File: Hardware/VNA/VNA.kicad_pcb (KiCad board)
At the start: 2 copper layers, 129 parts, among them J1 USB_B_Micro, J2 USB_A, J3 SMA, J4 SMA, U1 MAX2871, U10 SN74LVC1G139, U11 PE42440, U12 PE4257, U13 AD8302, U2 TVL755P, U3 LP5912, U4 MIC5366-1.8, U5 AD8319, U6 PE43711, U7 TRF37A75, U8 74AHC1G04, U9 PE42440, X1 ASTXR-12-19.200MHz

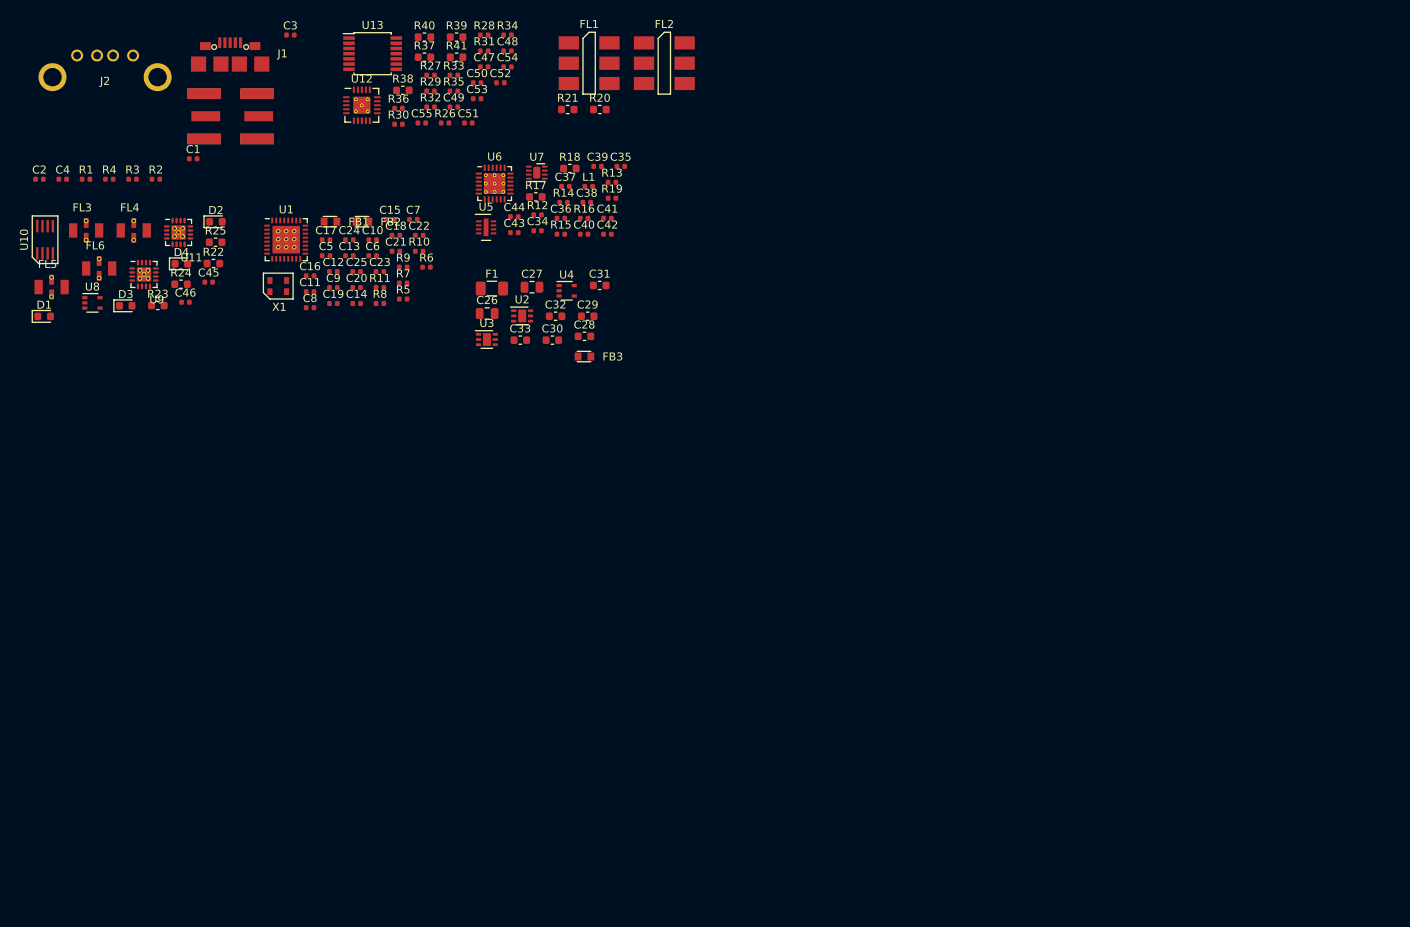
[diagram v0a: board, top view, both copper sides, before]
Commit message: all 3d models created, prelim bom generated
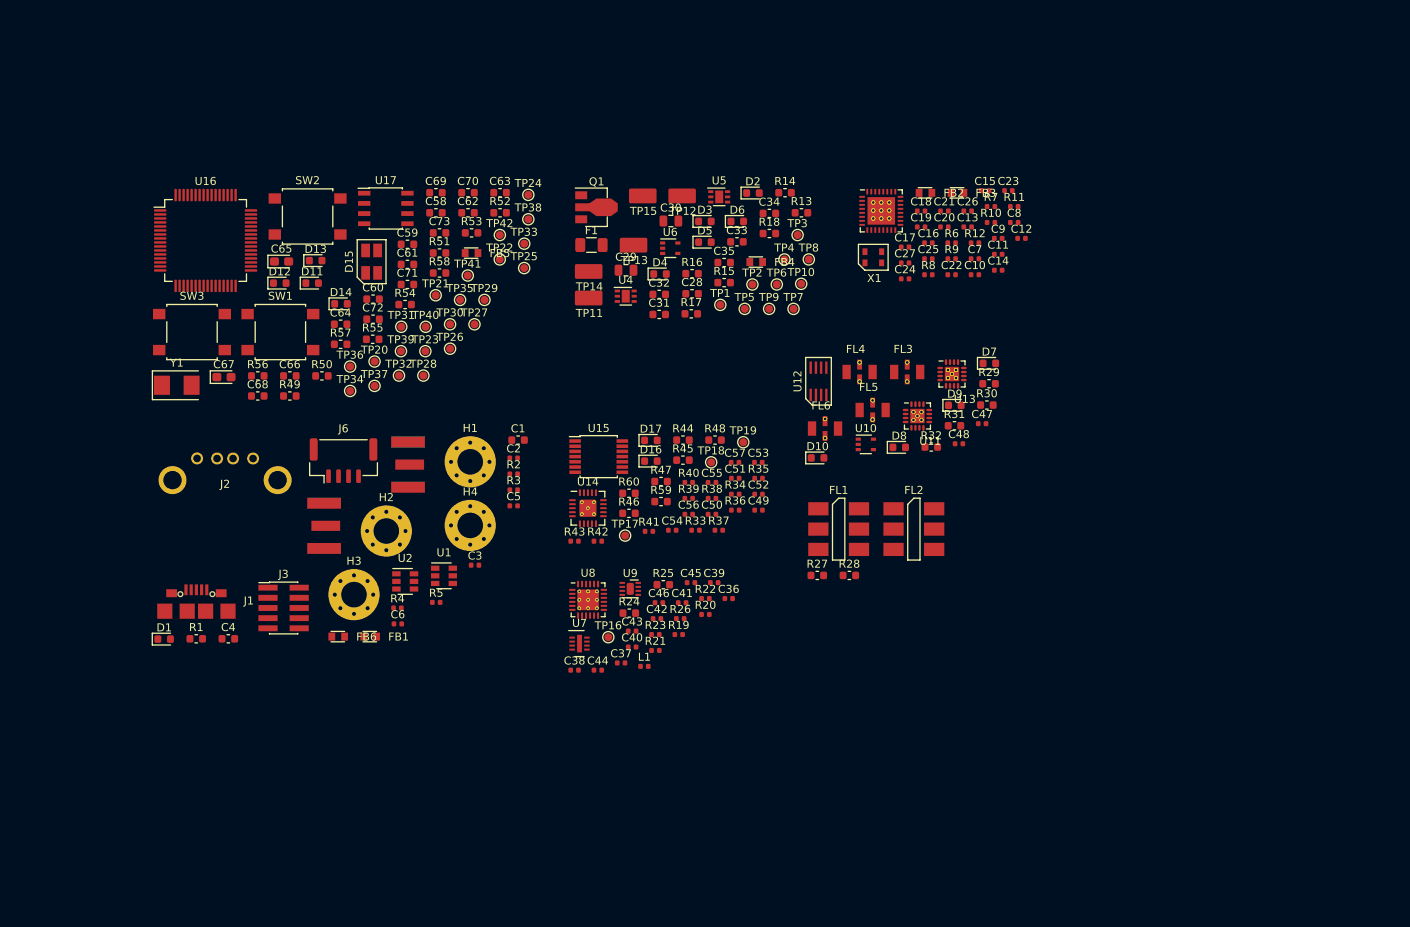
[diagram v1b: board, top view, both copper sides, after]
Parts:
- added C56: 100p, Capacitor_SMD:C_0402_1005Metric, F.Cu at (102.1, 78.8)
- added C57: DNP, Capacitor_SMD:C_0402_1005Metric, F.Cu at (107.9, 72.3)
- added C58: 1u, Capacitor_SMD:C_0603_1608Metric, F.Cu at (70.5, 41.1)
- added C59: 100n, Capacitor_SMD:C_0603_1608Metric, F.Cu at (67.0, 45.0)
- added C60: 10p, Capacitor_SMD:C_0603_1608Metric, F.Cu at (62.7, 51.9)
- added C61: 10p, Capacitor_SMD:C_0603_1608Metric, F.Cu at (67.0, 47.5)
- added C62: 1u, Capacitor_SMD:C_0603_1608Metric, F.Cu at (74.5, 41.1)
- added C63: 100n, Capacitor_SMD:C_0603_1608Metric, F.Cu at (78.5, 38.6)
- added C64: 100n, Capacitor_SMD:C_0603_1608Metric, F.Cu at (58.6, 55.0)
- added C65: 1u, Capacitor_Tantalum_SMD:CP_EIA-2012-15_AVX-P, F.Cu at (51.2, 47.2)
- added C66: 100n, Capacitor_SMD:C_0603_1608Metric, F.Cu at (52.3, 61.5)
- added C67: 1u, Capacitor_Tantalum_SMD:CP_EIA-2012-15_AVX-P, F.Cu at (44.0, 61.6)
- added C68: 100n, Capacitor_SMD:C_0603_1608Metric, F.Cu at (48.2, 64.0)
- added C69: 1u, Capacitor_SMD:C_0603_1608Metric, F.Cu at (70.5, 38.6)
- added C70: 100n, Capacitor_SMD:C_0603_1608Metric, F.Cu at (74.5, 38.6)
- added C71: 1u, Capacitor_SMD:C_0603_1608Metric, F.Cu at (67.0, 50.0)
- added C72: 100n, Capacitor_SMD:C_0603_1608Metric, F.Cu at (62.7, 54.4)
- added C73: 100n, Capacitor_SMD:C_0603_1608Metric, F.Cu at (71.0, 43.6)
- added D10: LED, LED_SMD:LED_0603_1608Metric, F.Cu at (118.2, 71.7)
- added D11: LED, LED_SMD:LED_0603_1608Metric, F.Cu at (55.0, 49.9)
- added D12: LED, LED_SMD:LED_0603_1608Metric, F.Cu at (51.0, 49.9)
- added D13: LED, LED_SMD:LED_0603_1608Metric, F.Cu at (55.5, 47.0)
- added D14: LED, LED_SMD:LED_0603_1608Metric, F.Cu at (58.6, 52.4)
- added D15: LED_RGBA, VNA_Footprints:ARGB_PLCC4_1210_LED, F.Cu at (62.5, 47.2)
- added D16: LED, LED_SMD:LED_0603_1608Metric, F.Cu at (97.4, 72.1)
- added D17: LED, LED_SMD:LED_0603_1608Metric, F.Cu at (97.4, 69.5)
- added D5: LED, LED_SMD:LED_0603_1608Metric, F.Cu at (104.1, 44.7)
- added D6: LED, LED_SMD:LED_0603_1608Metric, F.Cu at (108.2, 42.1)
- added D7: LED, LED_SMD:LED_0603_1608Metric, F.Cu at (139.7, 59.9)
- added D8: LED, LED_SMD:LED_0603_1608Metric, F.Cu at (128.4, 70.4)
- added D9: LED, LED_SMD:LED_0603_1608Metric, F.Cu at (135.4, 65.1)
- added FB4: Bead, VNA_Footprints:BEADC1608X95N, F.Cu at (110.6, 47.2)
- added FB5: Bead, VNA_Footprints:BEADC1608X95N, F.Cu at (75.0, 46.1)
- added FB6: Bead, VNA_Footprints:BEADC1608X95N, F.Cu at (58.3, 94.0)
- added H1: M3_Via_Pad, MountingHole:MountingHole_3.2mm_M3_Pad_Via, F.Cu at (74.8, 72.2)
- added H2: M3_Via_Pad, MountingHole:MountingHole_3.2mm_M3_Pad_Via, F.Cu at (64.3, 80.8)
- added H3: M3_Via_Pad, MountingHole:MountingHole_3.2mm_M3_Pad_Via, F.Cu at (60.3, 88.8)
- added H4: M3_Via_Pad, MountingHole:MountingHole_3.2mm_M3_Pad_Via, F.Cu at (74.8, 80.1)
- added J5: SMA, VNA_Footprints:SMA_EDGE_MOUNT, F.Cu at (56.5, 80.2)
- added J6: UART, Connector_JST:JST_GH_BM04B-GHS-TBT_1x04-1MP_P1.25mm_Vertical, F.Cu at (59.0, 72.0)
- added Q1: RE1C002UN, Package_TO_SOT_SMD:SOT-89-3, F.Cu at (90.2, 40.4)
- added R42: 52R3, Resistor_SMD:R_0402_1005Metric, F.Cu at (90.8, 82.1)
- added R43: 52R3, Resistor_SMD:R_0402_1005Metric, F.Cu at (87.8, 82.1)
- added R44: 0R0, Resistor_SMD:R_0603_1608Metric, F.Cu at (101.4, 69.5)
- added R45: 0R0, Resistor_SMD:R_0603_1608Metric, F.Cu at (101.4, 72.0)
- added R46: 0R0, Resistor_SMD:R_0603_1608Metric, F.Cu at (94.6, 78.6)
- added R47: 0R0, Resistor_SMD:R_0603_1608Metric, F.Cu at (98.7, 74.7)
- added R48: 0R0, Resistor_SMD:R_0603_1608Metric, F.Cu at (105.4, 69.5)
- added R49: DNP, Resistor_SMD:R_0603_1608Metric, F.Cu at (52.3, 64.0)
- added R50: 10K, Resistor_SMD:R_0603_1608Metric, F.Cu at (56.3, 61.5)
- added R51: 0R0, Resistor_SMD:R_0603_1608Metric, F.Cu at (71.0, 46.1)
- added R52: 470R, Resistor_SMD:R_0603_1608Metric, F.Cu at (78.5, 41.1)
- added R53: 470R, Resistor_SMD:R_0603_1608Metric, F.Cu at (75.0, 43.6)
- added R54: 470R, Resistor_SMD:R_0603_1608Metric, F.Cu at (66.7, 52.5)
- added R55: 470R, Resistor_SMD:R_0603_1608Metric, F.Cu at (62.6, 56.9)
- added R56: 0R0, Resistor_SMD:R_0603_1608Metric, F.Cu at (48.2, 61.5)
- added R57: 0R0, Resistor_SMD:R_0603_1608Metric, F.Cu at (58.6, 57.5)
- added R58: 1K5, Resistor_SMD:R_0603_1608Metric, F.Cu at (71.0, 48.6)
- added R59: 470R, Resistor_SMD:R_0603_1608Metric, F.Cu at (98.7, 77.2)
- added R60: 470R, Resistor_SMD:R_0603_1608Metric, F.Cu at (94.6, 76.1)
- added SW1: SW_Push, VNA_Footprints:6mmTactSwitch, F.Cu at (51.1, 56.0)
- added SW2: SW_Push, VNA_Footprints:6mmTactSwitch, F.Cu at (54.5, 41.5)
- added SW3: SW_Push, VNA_Footprints:6mmTactSwitch, F.Cu at (40.0, 56.0)
- added TP1: VBUS, TestPoint:TestPoint_Pad_D1.0mm, F.Cu at (106.1, 52.6)
- added TP10: GND, TestPoint:TestPoint_Pad_D1.0mm, F.Cu at (116.2, 49.9)
- added TP11: GND, VNA_Footprints:S1751-46_smdTestPoint, F.Cu at (89.6, 51.7)
- added TP12: GND, VNA_Footprints:S1751-46_smdTestPoint, F.Cu at (101.3, 39.0)
- added TP13: GND, VNA_Footprints:S1751-46_smdTestPoint, F.Cu at (95.2, 45.1)
- added TP14: GND, VNA_Footprints:S1751-46_smdTestPoint, F.Cu at (89.6, 48.4)
- added TP15: GND, VNA_Footprints:S1751-46_smdTestPoint, F.Cu at (96.4, 39.0)
- added TP16: TP, TestPoint:TestPoint_Pad_D1.0mm, F.Cu at (92.1, 94.1)
- added TP17: TP, TestPoint:TestPoint_Pad_D1.0mm, F.Cu at (94.2, 81.4)
- added TP18: TP, TestPoint:TestPoint_Pad_D1.0mm, F.Cu at (104.9, 72.3)
- added TP19: TP, TestPoint:TestPoint_Pad_D1.0mm, F.Cu at (108.9, 69.7)
- added TP2: 5V0, TestPoint:TestPoint_Pad_D1.0mm, F.Cu at (110.1, 50.0)
- added TP20: TP, TestPoint:TestPoint_Pad_D1.0mm, F.Cu at (62.8, 59.7)
- added TP21: TP, TestPoint:TestPoint_Pad_D1.0mm, F.Cu at (70.5, 51.4)
- added TP22: TP, TestPoint:TestPoint_Pad_D1.0mm, F.Cu at (78.5, 46.9)
- added TP23: TP, TestPoint:TestPoint_Pad_D1.0mm, F.Cu at (69.2, 58.4)
- added TP24: TP, TestPoint:TestPoint_Pad_D1.0mm, F.Cu at (82.1, 38.8)
- added TP25: TP, TestPoint:TestPoint_Pad_D1.0mm, F.Cu at (81.5, 48.0)
- added TP26: TP, TestPoint:TestPoint_Pad_D1.0mm, F.Cu at (72.3, 58.1)
- added TP27: TP, TestPoint:TestPoint_Pad_D1.0mm, F.Cu at (75.3, 55.0)
- added TP28: TP, TestPoint:TestPoint_Pad_D1.0mm, F.Cu at (68.9, 61.4)
- added TP29: TP, TestPoint:TestPoint_Pad_D1.0mm, F.Cu at (76.6, 52.0)
- added TP3: 3V3A, TestPoint:TestPoint_Pad_D1.0mm, F.Cu at (115.7, 43.8)
- added TP30: TP, TestPoint:TestPoint_Pad_D1.0mm, F.Cu at (72.3, 55.0)
- added TP31: TP, TestPoint:TestPoint_Pad_D1.0mm, F.Cu at (66.2, 55.3)
- added TP32: TP, TestPoint:TestPoint_Pad_D1.0mm, F.Cu at (65.9, 61.4)
- added TP33: TP, TestPoint:TestPoint_Pad_D1.0mm, F.Cu at (81.6, 44.9)
- added TP34: TP, TestPoint:TestPoint_Pad_D1.0mm, F.Cu at (59.8, 63.3)
- added TP35: TP, TestPoint:TestPoint_Pad_D1.0mm, F.Cu at (73.5, 52.0)
- added TP36: TP, TestPoint:TestPoint_Pad_D1.0mm, F.Cu at (59.8, 60.3)
- added TP37: TP, TestPoint:TestPoint_Pad_D1.0mm, F.Cu at (62.8, 62.7)
- added TP38: TP, TestPoint:TestPoint_Pad_D1.0mm, F.Cu at (82.1, 41.9)
- added TP39: TP, TestPoint:TestPoint_Pad_D1.0mm, F.Cu at (66.1, 58.4)
- added TP4: 1V8, TestPoint:TestPoint_Pad_D1.0mm, F.Cu at (114.1, 46.9)
- added TP40: TP, TestPoint:TestPoint_Pad_D1.0mm, F.Cu at (69.2, 55.3)
- added TP41: TP, TestPoint:TestPoint_Pad_D1.0mm, F.Cu at (74.5, 48.9)
- added TP42: TP, TestPoint:TestPoint_Pad_D1.0mm, F.Cu at (78.5, 43.8)
- added TP5: 3V3, TestPoint:TestPoint_Pad_D1.0mm, F.Cu at (109.1, 53.1)
- added TP6: GND, TestPoint:TestPoint_Pad_D1.0mm, F.Cu at (113.1, 50.0)
- added TP7: GND, TestPoint:TestPoint_Pad_D1.0mm, F.Cu at (115.2, 53.1)
- added TP8: GND, TestPoint:TestPoint_Pad_D1.0mm, F.Cu at (117.1, 46.9)
- added TP9: GND, TestPoint:TestPoint_Pad_D1.0mm, F.Cu at (112.2, 53.1)
- added U14: PE4257, VNA_Footprints:QFN-20-1EP_4x4mm_P0.5mm_EP2.15x2.15mm_ThermalVias, F.Cu at (89.5, 78.0)
- added U15: AD8302, Package_SO:TSSOP-14_4.4x5mm_P0.65mm, F.Cu at (90.9, 71.5)
- added U16: STM32F373RCTx, Package_QFP:LQFP-64_10x10mm_P0.5mm, F.Cu at (41.7, 44.5)
- added U17: AT25SF081-SSHD-X, Package_SO:SOIC-8_3.9x4.9mm_P1.27mm, F.Cu at (64.3, 40.5)
- added Y1: 8MHz, VNA_Footprints:Crystal_SMD_5032-2Pin_5.0x3.2mm, F.Cu at (38.1, 62.6)
- C1, C4: value 1n -> 100n; footprint Capacitor_SMD:C_0402_1005Metric -> Capacitor_SMD:C_0603_1608Metric
- C10: value 10n -> 1u
- C11: value 100p -> 1u
- C22: value 100n -> 10n
- C23: value 12n -> 100p
- C24: value 820p -> 100n
- C25: value 100p -> 12n
- C26: value 10u -> 820p; footprint Capacitor_SMD:C_0805_2012Metric -> Capacitor_SMD:C_0402_1005Metric
- C27: value 10u -> 100p; footprint Capacitor_SMD:C_0805_2012Metric -> Capacitor_SMD:C_0402_1005Metric
- C29, C30: value 1u -> 10u; footprint Capacitor_SMD:C_0603_1608Metric -> Capacitor_SMD:C_0805_2012Metric
- C34: value 8.2p -> 1u; footprint Capacitor_SMD:C_0402_1005Metric -> Capacitor_SMD:C_0603_1608Metric
- C35: value 47n -> 1u; footprint Capacitor_SMD:C_0402_1005Metric -> Capacitor_SMD:C_0603_1608Metric
- C36: value 100n -> 8.2p
- C37, C40: value 100p -> 47n
- C38: value 47n -> 100n
- C39: value 100n -> 100p
- C41: value 1n -> 100n
- C42: value 10n -> 100p
- C43, C6: value 10n -> 1n
- C44: value 10p -> 10n
- C46: value 10n -> 10p
- C48, C49: value 1n -> 10n
- C5, C53: value 100n -> 1n
- C52: value DNP -> 1n
- C54: value 100p -> DNP
- C55: value DNP -> 100n
- C7: value 1u -> 100n
- C8: value 1u -> 10n
- F1: footprint Fuse:Fuse_1206_3216Metric -> VNA_Footprints:Fuse_1206_3216Metric
- FB1, FB2, FB3: value BLM18PG181SN1D -> Bead
- J3: value SMA -> Conn_ARM_SWD; footprint VNA_Footprints:SMA_EDGE_MOUNT -> VNA_Footprints:SAMTEC_FTSH-105-01-L-DV-R-TR
- R1: value 49R9 -> 470R; footprint Resistor_SMD:R_0402_1005Metric -> Resistor_SMD:R_0603_1608Metric
- R10: value 240 -> 31.1
- R11: value 49.9 -> 240
- R12: value 18k -> 49.9
- R13: value 52.3 -> 10K; footprint Resistor_SMD:R_0402_1005Metric -> Resistor_SMD:R_0603_1608Metric
- R14: value 0 -> 470R; footprint Resistor_SMD:R_0402_1005Metric -> Resistor_SMD:R_0603_1608Metric
- R15: value OPT -> 470R; footprint Resistor_SMD:R_0402_1005Metric -> Resistor_SMD:R_0603_1608Metric
- R16: value 1k -> 470R; footprint Resistor_SMD:R_0402_1005Metric -> Resistor_SMD:R_0603_1608Metric
- R17: value 0R -> 1K
- R18: value DNP -> 1K
- R19: value 1R8 -> 18k
- R2: value 16R6 -> 49R9
- R20: value 49R9 -> 52.3; footprint Resistor_SMD:R_0603_1608Metric -> Resistor_SMD:R_0402_1005Metric
- R21: value 49R9 -> 0; footprint Resistor_SMD:R_0603_1608Metric -> Resistor_SMD:R_0402_1005Metric
- R22: value 470R -> OPT; footprint Resistor_SMD:R_0603_1608Metric -> Resistor_SMD:R_0402_1005Metric
- R23: value 470R -> 1k; footprint Resistor_SMD:R_0603_1608Metric -> Resistor_SMD:R_0402_1005Metric
- R24: value 470R -> 0R
- R25: value 470R -> DNP
- R26: value DNP -> 1R8
- R27: value 150R -> 49R9; footprint Resistor_SMD:R_0402_1005Metric -> Resistor_SMD:R_0603_1608Metric
- R28: value 60R -> 49R9; footprint Resistor_SMD:R_0402_1005Metric -> Resistor_SMD:R_0603_1608Metric
- R29: value 0R0 -> 470R; footprint Resistor_SMD:R_0402_1005Metric -> Resistor_SMD:R_0603_1608Metric
- R30: value 37R -> 470R; footprint Resistor_SMD:R_0402_1005Metric -> Resistor_SMD:R_0603_1608Metric
- R31: value 278R -> 470R; footprint Resistor_SMD:R_0402_1005Metric -> Resistor_SMD:R_0603_1608Metric
- R32: value DNP -> 470R; footprint Resistor_SMD:R_0402_1005Metric -> Resistor_SMD:R_0603_1608Metric
- R33: value 150R -> DNP
- R34: value 60R -> 150R
- R35: value 52R3 -> 60R
- R36: value 52R3 -> 0R0
- R37: value 0R0 -> 37R; footprint Resistor_SMD:R_0603_1608Metric -> Resistor_SMD:R_0402_1005Metric
- R38: value 0R0 -> 278R; footprint Resistor_SMD:R_0603_1608Metric -> Resistor_SMD:R_0402_1005Metric
- R39: value 0R0 -> DNP; footprint Resistor_SMD:R_0603_1608Metric -> Resistor_SMD:R_0402_1005Metric
- R40: value 0R0 -> 150R; footprint Resistor_SMD:R_0603_1608Metric -> Resistor_SMD:R_0402_1005Metric
- R41: value 0R0 -> 60R; footprint Resistor_SMD:R_0603_1608Metric -> Resistor_SMD:R_0402_1005Metric
- R5: value 5.1k -> 16R6
- R6: value 0 -> 5.1k
- R8: value 90.9 -> 0
- R9: value 31.1 -> 90.9
- U1: value MAX2871 -> TPD2S017; footprint VNA_Footprints:QFN-32-1EP_5x5mm_Pitch0.5mm_Thermal_Vias -> Package_TO_SOT_SMD:SOT-23-6
- U10: value SN74LVC1G139 -> 74AHC1G04; footprint VNA_Footprints:VSSOP-8_2.9x3.15mm_P0.65 -> Package_TO_SOT_SMD:SOT-353_SC-70-5
- U12: value PE4257 -> SN74LVC1G139; footprint VNA_Footprints:QFN-20-1EP_4x4mm_P0.5mm_EP2.15x2.15mm_ThermalVias -> VNA_Footprints:VSSOP-8_2.9x3.15mm_P0.65
- U13: value AD8302 -> PE42440; footprint Package_SO:TSSOP-14_4.4x5mm_P0.65mm -> VNA_Footprints:QFN-16-1EP_3x3mm_P0.5mm_EP2.7x2.7mm_ThermalVias
- U2: value TVL755P -> TPD2S017; footprint Package_DFN_QFN:DFN-6-1EP_2x2mm_P0.65mm_EP1x1.6mm -> Package_TO_SOT_SMD:SOT-23-6
- U3: value LP5912 -> MAX2871; footprint Package_DFN_QFN:DFN-6-1EP_2x2mm_P0.65mm_EP1x1.6mm -> VNA_Footprints:QFN-32-1EP_5x5mm_Pitch0.5mm_Thermal_Vias
- U4: value MIC5366-1.8 -> LP5912; footprint Package_TO_SOT_SMD:SOT-353_SC-70-5 -> Package_DFN_QFN:DFN-6-1EP_2x2mm_P0.65mm_EP1x1.6mm
- U5: value AD8319 -> TVL755P; footprint Package_DFN_QFN:DFN-8-1EP_2x3mm_P0.5mm_EP0.61x2.2mm -> Package_DFN_QFN:DFN-6-1EP_2x2mm_P0.65mm_EP1x1.6mm
- U6: value PE43711 -> MIC5366-1.8; footprint VNA_Footprints:QFN-24-1EP_4x4mm_P0.5mm_EP2.7x2.6mm_ThermalVias -> Package_TO_SOT_SMD:SOT-353_SC-70-5
- U7: value TRF37A75 -> AD8319; footprint Package_DFN_QFN:DFN-8-1EP_2x2mm_P0.5mm_EP0.9x1.5mm -> Package_DFN_QFN:DFN-8-1EP_2x3mm_P0.5mm_EP0.61x2.2mm
- U8: value 74AHC1G04 -> PE43711; footprint Package_TO_SOT_SMD:SOT-353_SC-70-5 -> VNA_Footprints:QFN-24-1EP_4x4mm_P0.5mm_EP2.7x2.6mm_ThermalVias
- U9: value PE42440 -> TRF37A75; footprint VNA_Footprints:QFN-16-1EP_3x3mm_P0.5mm_EP2.7x2.7mm_ThermalVias -> Package_DFN_QFN:DFN-8-1EP_2x2mm_P0.5mm_EP0.9x1.5mm
- moved U10 105.7 mm to (124.3, 70.0)
- moved FL3 104.1 mm to (129.4, 61.0)
- moved FL5 103.8 mm to (125.1, 65.7)
- moved U11 95.2 mm to (130.7, 66.5)
- moved FL6 92.9 mm to (119.2, 68.0)
- moved FL4 92.4 mm to (123.5, 61.0)
- moved C8 88.7 mm to (142.8, 42.3)
- moved C11 86.1 mm to (140.8, 46.3)
- moved C12 86.1 mm to (143.7, 44.3)
- moved C9 83.3 mm to (140.8, 44.3)
- moved U13 82.8 mm to (135.0, 61.2)
- moved R28 81.5 mm to (122.2, 86.4)
- moved R30 81.5 mm to (139.4, 65.1)
- moved C14 80.3 mm to (140.8, 48.2)
- moved R11 79.9 mm to (142.8, 40.3)
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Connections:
- C1 pad 2: /Synth/RF_OUT_N -> GND
- C10 pad 1: /3V3 -> Net-(C10-Pad1)
- C11 pad 1: /3V3 -> Net-(C11-Pad1)
- C12 pad 1: /3V3 -> VDD
- C13 pad 1: /3V3 -> VDD
- C14 pad 1: Net-(C14-Pad1) -> VDD
- C15 pad 1: Net-(C14-Pad1) -> VDD
- C16 pad 1: Net-(C14-Pad1) -> Net-(C16-Pad1)
- C17 pad 1: Net-(C14-Pad1) -> Net-(C16-Pad1)
- C18 pad 1: Net-(C18-Pad1) -> Net-(C16-Pad1)
- C19 pad 1: Net-(C18-Pad1) -> Net-(C16-Pad1)
- C2 pad 1: /Filter Bank/RF_IN -> Net-(C2-Pad1)
- C2 pad 2: /Synth/RF_OUT_P -> /Synth/RF_OUT_N
- C20 pad 1: Net-(C18-Pad1) -> Net-(C20-Pad1)
- C21 pad 1: Net-(C18-Pad1) -> Net-(C20-Pad1)
- C22 pad 1: Net-(C22-Pad1) -> Net-(C20-Pad1)
- C22 pad 2: Net-(C22-Pad2) -> GND
- C23 pad 1: Net-(C22-Pad2) -> Net-(C20-Pad1)
- C24 pad 2: GND -> Net-(C24-Pad2)
- C25 pad 1: /3V3A -> Net-(C24-Pad2)
- C26 pad 1: /Power/VIN -> Net-(C26-Pad1)
- C27 pad 1: /5V0 -> /3V3A
- C29 pad 1: /3V3 -> /Power/VIN
- C3 pad 1: /Source Leveling/RF_IN -> /Filter Bank/RF_IN
- C3 pad 2: /Filter Bank/RF_OUT -> /Synth/RF_OUT_P
- C30 pad 1: /Power/VIN -> /5V0
- C32 pad 1: /3V3A -> /Power/VIN
- C33 pad 1: /1V8 -> /3V3A
- C34 pad 1: Net-(C34-Pad1) -> VDD
- C35 pad 1: /AD8319_RF -> /1V8
- C35 pad 2: Net-(C35-Pad2) -> GND
- C36 pad 1: GND -> Net-(C36-Pad1)
- C36 pad 2: /3V3A -> GND
- C37 pad 1: GND -> /AD8319_RF
- C37 pad 2: /3V3A -> Net-(C37-Pad2)
- C38 pad 2: Net-(C38-Pad2) -> /3V3A
- C4 pad 1: /Directional Couplers/RF_IN -> Net-(C4-Pad1)
- C4 pad 2: /Source Leveling/RF_OUT -> GND
- C40 pad 2: /3V3A -> Net-(C40-Pad2)
- C41 pad 1: Net-(C41-Pad1) -> GND
- C41 pad 2: Net-(C41-Pad2) -> /3V3A
- C42 pad 1: /5V0 -> GND
- C42 pad 2: GND -> /3V3A
- C43 pad 1: /5V0 -> Net-(C43-Pad1)
- C43 pad 2: GND -> Net-(C43-Pad2)
- C44 pad 1: Net-(C44-Pad1) -> /5V0
- C45 pad 1: GND -> /5V0
- C45 pad 2: /3V3A -> GND
- C46 pad 1: GND -> Net-(C46-Pad1)
- C46 pad 2: /3V3A -> GND
- C47 pad 2: /3V3 -> /3V3A
- C48 pad 1: Net-(C48-Pad1) -> GND
- C48 pad 2: Net-(C48-Pad2) -> /3V3A
- C49 pad 1: Net-(C49-Pad1) -> GND
- C49 pad 2: GND -> /3V3A
- C5 pad 1: /1V8 -> /Source Leveling/RF_IN
- C5 pad 2: GND -> /Filter Bank/RF_OUT
- C50 pad 2: GND -> Net-(C50-Pad2)
- C51 pad 2: Net-(C51-Pad2) -> GND
- C53 pad 1: GND -> Net-(C53-Pad1)
- C53 pad 2: /3V3 -> Net-(C53-Pad2)
- C54 pad 1: GND -> Net-(C54-Pad1)
- C54 pad 2: /3V3 -> GND
- C55 pad 1: Net-(C55-Pad1) -> GND
- C55 pad 2: GND -> /3V3A
- C6 pad 1: Net-(C6-Pad1) -> /Directional Couplers/RF_IN
- C6 pad 2: Net-(C6-Pad2) -> /Source Leveling/RF_OUT
- C7 pad 1: Net-(C7-Pad1) -> /1V8
- C8 pad 2: GND -> Net-(C8-Pad2)
- D1 pad 1: Net-(D1-Pad1) -> GND
- D3 pad 1: Net-(D3-Pad1) -> GND
- D4 pad 1: Net-(D4-Pad1) -> GND
- FB1 pad 1: Net-(C14-Pad1) -> /VBUS
- FB1 pad 2: /3V3A -> Net-(C1-Pad1)
- FB2 pad 1: Net-(C18-Pad1) -> Net-(C16-Pad1)
- FB3 pad 1: /5V0 -> Net-(C20-Pad1)
- FB3 pad 2: /Power/VIN -> /3V3A
- J1 pad 1: /VBUS -> Net-(C1-Pad1)
- J1 pad 2: (no net) -> /Dn
- J1 pad 3: (no net) -> /Dp
- J2 pad 1: /5V0 -> Net-(C4-Pad1)
- J2 pad 2: (no net) -> Net-(J2-Pad2)
- J2 pad 3: (no net) -> Net-(J2-Pad3)
- J3 pad 1: /RF_THROUGH -> VDD
- J3 pad 2: GND -> /SWD_IO
- J4 pad 1: /Directional Couplers/RF_OUT -> /RF_THROUGH
- L1 pad 1: Net-(C44-Pad1) -> Net-(C46-Pad1)
- R1 pad 1: Net-(C1-Pad1) -> /MAX2871_LD
- R1 pad 2: GND -> Net-(D1-Pad2)
- R10 pad 1: Net-(C22-Pad2) -> Net-(R10-Pad1)
- R11 pad 1: /3V3A -> Net-(C24-Pad2)
- R11 pad 2: /Synth/RF_OUT_P -> Net-(C26-Pad1)
- R12 pad 1: Net-(R12-Pad1) -> /3V3A
- R12 pad 2: GND -> /Synth/RF_OUT_P
- R13 pad 1: GND -> /1V8
- R13 pad 2: /AD8319_RF -> GND
- R14 pad 1: Net-(R14-Pad1) -> /3V3A
- R14 pad 2: Net-(R14-Pad2) -> Net-(D2-Pad2)
- R15 pad 1: Net-(R14-Pad2) -> /3V3A
- R15 pad 2: GND -> Net-(D3-Pad2)
- R16 pad 1: (no net) -> VDD
- R16 pad 2: Net-(R14-Pad1) -> Net-(D4-Pad2)
- R17 pad 1: /3V3A -> /5V0
- R17 pad 2: /Source Leveling/nP_S -> Net-(D5-Pad2)
- R18 pad 1: /Source Leveling/nP_S -> /VBUS
- R18 pad 2: GND -> Net-(D6-Pad2)
- R19 pad 1: /5V0 -> Net-(R19-Pad1)
- R19 pad 2: Net-(C44-Pad1) -> GND
- R2 pad 1: Net-(R2-Pad1) -> Net-(C2-Pad1)
- R2 pad 2: /AD8319_RF -> GND
- R20 pad 1: Net-(FL1-Pad4) -> GND
- R20 pad 2: GND -> /AD8319_RF
- R21 pad 1: Net-(FL2-Pad4) -> Net-(R21-Pad1)
- R21 pad 2: GND -> Net-(R21-Pad2)
- R22 pad 1: Net-(D1-Pad2) -> Net-(R21-Pad2)
- R22 pad 2: /3V3 -> GND
- R23 pad 1: Net-(D2-Pad2) -> /RF_PWR_LEVEL
- R23 pad 2: /3V3 -> Net-(R21-Pad1)
- R24 pad 1: Net-(D3-Pad2) -> /3V3A
- R24 pad 2: /3V3 -> /Source Leveling/nP_S
- R25 pad 1: Net-(D4-Pad2) -> /Source Leveling/nP_S
- R25 pad 2: /3V3 -> GND
- R26 pad 1: /RF_FWD_CPL -> /5V0
- R26 pad 2: GND -> Net-(C46-Pad1)
- R27 pad 1: /RF_REV_CPL -> Net-(FL1-Pad4)
- R28 pad 1: /RF_THROUGH -> Net-(FL2-Pad4)
- R29 pad 1: Net-(C48-Pad2) -> Net-(D7-Pad2)
- R29 pad 2: /RF_FWD_CPL -> VDD
- R3 pad 1: /Directional Couplers/Forward_CPL -> Net-(R3-Pad1)
- R3 pad 2: Net-(R2-Pad1) -> /AD8319_RF
- R30 pad 1: Net-(R30-Pad1) -> Net-(D8-Pad2)
- R30 pad 2: /RF_REV_CPL -> VDD
- R31 pad 1: Net-(R31-Pad1) -> Net-(D9-Pad2)
- R31 pad 2: /RF_THROUGH -> VDD
- R32 pad 1: Net-(C48-Pad2) -> Net-(D10-Pad2)
- R32 pad 2: GND -> VDD
- R33 pad 1: Net-(R30-Pad1) -> /RF_FWD_CPL
- R34 pad 1: Net-(R31-Pad1) -> /RF_REV_CPL
- R35 pad 1: Net-(C48-Pad2) -> /RF_THROUGH
- R36 pad 1: Net-(C51-Pad2) -> Net-(C50-Pad2)
- R36 pad 2: GND -> /RF_FWD_CPL
- R37 pad 2: Net-(R37-Pad2) -> /RF_REV_CPL
- R38 pad 2: Net-(R38-Pad2) -> /RF_THROUGH
- R39 pad 1: (no net) -> Net-(C50-Pad2)
- R39 pad 2: Net-(R37-Pad1) -> GND
- R4 pad 1: /RF_FWD_CPL -> /Directional Couplers/Forward_CPL
- R4 pad 2: Net-(R2-Pad1) -> Net-(R3-Pad1)
- R40 pad 1: (no net) -> Net-(R37-Pad1)
- R40 pad 2: Net-(R40-Pad2) -> GND
- R41 pad 1: (no net) -> Net-(R38-Pad1)
- R41 pad 2: Net-(R38-Pad1) -> GND
- R5 pad 1: Net-(R5-Pad1) -> /RF_FWD_CPL
- R5 pad 2: GND -> Net-(R3-Pad1)
- R6 pad 1: /3V3A -> Net-(R6-Pad1)
- R6 pad 2: Net-(R6-Pad2) -> GND
- R8 pad 1: Net-(R8-Pad1) -> /3V3A
- R8 pad 2: GND -> Net-(R8-Pad2)
- R9 pad 1: Net-(R8-Pad1) -> Net-(R10-Pad1)
- R9 pad 2: Net-(C22-Pad1) -> GND
- U1 pad 1: (no net) -> /USB_D+
- U1 pad 2: (no net) -> GND
- U1 pad 3: (no net) -> /Dp
- U1 pad 4: (no net) -> /Dn
- U1 pad 5: Net-(R8-Pad1) -> /VBUS
- U1 pad 6: Net-(C14-Pad1) -> /USB_D-
- U10 pad 1: /Filter_CTRL1 -> (no net)
- U10 pad 2: /Filter_CTRL2 -> /Filter_CTRL1
- U10 pad 3: Net-(D4-Pad1) -> GND
- U10 pad 4: GND -> /Filter Bank/SW_2_CTRL_1
- U10 pad 5: Net-(D3-Pad1) -> /3V3A
- U11 pad 11: /Filter Bank/RF_OUT -> /Filter Bank/RF_IN
- U11 pad 13: /Filter Bank/SW_2_RF_1 -> /Filter Bank/SW_1_RF_1
- U11 pad 15: /Filter Bank/SW_2_RF_2 -> /Filter Bank/SW_1_RF_2
- U11 pad 4: /Filter Bank/SW_2_CTRL_1 -> /Filter_CTRL1
- U11 pad 6: /Filter Bank/SW_2_RF_4 -> /Filter Bank/SW_1_RF_4
- U11 pad 8: /Filter Bank/SW_2_RF_3 -> /Filter Bank/SW_1_RF_3
- U12 pad 1: GND -> /Filter_CTRL1
- U12 pad 2: GND -> /Filter_CTRL2
- U12 pad 3: Net-(R30-Pad1) -> Net-(D10-Pad1)
- U12 pad 5: GND -> Net-(D9-Pad1)
- U12 pad 6: GND -> Net-(D8-Pad1)
- U12 pad 7: GND -> Net-(D7-Pad1)
- U12 pad 8: Net-(C51-Pad2) -> VDD
- U13 pad 10: Net-(R38-Pad2) -> GND
- U13 pad 11: Net-(R40-Pad2) -> /Filter Bank/RF_OUT
- U13 pad 12: Net-(R37-Pad2) -> GND
- U13 pad 13: Net-(R37-Pad1) -> /Filter Bank/SW_2_RF_1
- U13 pad 14: Net-(C55-Pad1) -> GND
- U13 pad 2: Net-(C48-Pad1) -> /3V3A
- U13 pad 3: Net-(C49-Pad1) -> /Filter_CTRL2
- U13 pad 4: /3V3 -> /Filter Bank/SW_2_CTRL_1
- U13 pad 5: Net-(C50-Pad1) -> GND
- U13 pad 6: Net-(C51-Pad1) -> /Filter Bank/SW_2_RF_4
- U13 pad 8: Net-(C52-Pad1) -> /Filter Bank/SW_2_RF_3
- U13 pad 9: Net-(R38-Pad1) -> GND
- U2 pad 1: /3V3 -> /SDA
- U2 pad 3: GND -> Net-(J2-Pad3)
- U2 pad 4: /Power/VIN -> Net-(J2-Pad2)
- U2 pad 5: GND -> /5V0
- U2 pad 6: /Power/VIN -> /SCL
- U3 pad 1: /3V3A -> /MAX2871_CLK
- U3 pad 2: GND -> /MAX2871_MOSI
- U3 pad 3: (no net) -> /MAX2871_LE
- U3 pad 4: /Power/VIN -> /MAX2871_CHIP_EN
- U3 pad 5: GND -> Net-(R10-Pad1)
- U3 pad 6: /Power/VIN -> Net-(C16-Pad1)
- U3 pad 7: GND -> Net-(C24-Pad2)
- U4 pad 3: /3V3A -> (no net)
- U4 pad 4: (no net) -> /Power/VIN
- U4 pad 5: /1V8 -> GND
- U5 pad 1: Net-(C35-Pad2) -> VDD
- U5 pad 3: Net-(C34-Pad1) -> GND
- U5 pad 4: Net-(R14-Pad2) -> /Power/VIN
- U5 pad 5: Net-(R14-Pad1) -> GND
- U5 pad 6: Net-(R12-Pad1) -> /Power/VIN
- U5 pad 7: /3V3A -> GND
- U6 pad 1: (no net) -> /3V3A
- U6 pad 2: /3V3A -> GND
- U6 pad 3: /Source Leveling/nP_S -> /3V3A
- U6 pad 4: GND -> (no net)
- U6 pad 5: /Source Leveling/RF_IN -> /1V8
- U7 pad 1: /5V0 -> Net-(C37-Pad2)
- U7 pad 2: Net-(C41-Pad1) -> GND
- U7 pad 3: GND -> Net-(C36-Pad1)
- U7 pad 4: GND -> Net-(R21-Pad2)
- U7 pad 5: (no net) -> Net-(R21-Pad1)
- U7 pad 6: GND -> Net-(R19-Pad1)
- U7 pad 7: /Source Leveling/RF_OUT -> /3V3A
- U7 pad 8: GND -> Net-(C40-Pad2)
- U8 pad 2: /Filter_CTRL1 -> /3V3A
- U8 pad 3: GND -> /Source Leveling/nP_S
- U8 pad 4: /Filter Bank/SW_2_CTRL_1 -> GND
- U8 pad 5: /3V3A -> /Source Leveling/RF_IN
- U9 pad 1: GND -> /5V0
- U9 pad 2: /3V3A -> Net-(C43-Pad1)
- U9 pad 3: /Filter_CTRL2 -> GND
- U9 pad 4: /Filter_CTRL1 -> GND
- U9 pad 5: GND -> /PA_PWRDN
- U9 pad 6: /Filter Bank/SW_1_RF_4 -> GND
- U9 pad 7: GND -> /Source Leveling/RF_OUT
- U9 pad 8: /Filter Bank/SW_1_RF_3 -> GND
- X1 pad 4: Net-(C6-Pad2) -> Net-(C8-Pad2)

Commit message: More schematic changes + updated functionals
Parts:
- added R61: 0R0, Resistor_SMD:R_0603_1608Metric, F.Cu at (48.8, 82.8)
- added REF**: SLP3-150-150-F, VNA_Footprints:SLP3-150-150-F, F.Cu at (44.7, 19.8)
- added TP43: 5V_VIN, VNA_Footprints:TestPoint_Loop_D1.80mm_Drill1.0mm_Beaded_RED, F.Cu at (61.9, 75.3)
- added TP44: TP, TestPoint:TestPoint_Pad_D1.0mm, F.Cu at (69.0, 32.6)
- C60, C61: footprint Capacitor_SMD:C_0603_1608Metric -> Capacitor_SMD:C_0402_1005Metric
- R24: value 0R -> 0R0
- U14: value PE4257 -> F2923; footprint VNA_Footprints:QFN-20-1EP_4x4mm_P0.5mm_EP2.15x2.15mm_ThermalVias -> VNA_Footprints:QFN-20-1EP_4x4mm_P0.5mm_EP2x2mm_ThermalVias
- U5: value TVL755P -> LP5912
- U8: value PE43711 -> SKY12347-362LF; footprint VNA_Footprints:QFN-24-1EP_4x4mm_P0.5mm_EP2.7x2.6mm_ThermalVias -> Package_DFN_QFN:QFN-24-1EP_4x4mm_P0.5mm_EP2.7x2.7mm_ThermalVias
- moved C1 51.6 mm to (31.1, 83.1)
- moved R52 41.5 mm to (38.7, 52.8)
- moved R49 37.6 mm to (61.0, 27.4)
- moved FB6 33.7 mm to (71.3, 63.0)
- moved R50 31.9 mm to (61.0, 29.9)
- moved C69 31.2 mm to (42.8, 52.8)
- moved D7 30.3 mm to (109.4, 60.5)
- moved D15 29.0 mm to (49.9, 21.0)
- moved C60 29.0 mm to (33.7, 52.8)
- moved TP34 28.8 mm to (68.0, 35.7)
- moved R51 28.5 mm to (42.8, 50.3)
- moved TP39 28.4 mm to (72.6, 30.7)
- moved R57 28.4 mm to (65.0, 29.9)
- moved TP32 28.4 mm to (72.1, 33.7)
- moved TP22 28.3 mm to (50.3, 49.1)
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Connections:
- J1 pad 1: Net-(C1-Pad1) -> Net-(J1-Pad1)
- R24 pad 2: /Source Leveling/nP_S -> Net-(R24-Pad2)
- R25 pad 1: /Source Leveling/nP_S -> Net-(R24-Pad2)
- TP27 pad 1: /ATTEN_DATA -> /ATTEN_MISO
- U16 pad 48: (no net) -> /ATTEN_MISO
- U16 pad 51: /ATTEN_DATA -> /ATTEN_MOSI
- U8 pad 1: (no net) -> Net-(R24-Pad2)
- U8 pad 13: GND -> Net-(C43-Pad2)
- U8 pad 14: Net-(C43-Pad2) -> GND
- U8 pad 15: GND -> /ATTEN_MISO
- U8 pad 16: /ATTEN_LE -> GND
- U8 pad 17: /ATTEN_CLK -> GND
- U8 pad 18: /ATTEN_DATA -> /3V3A
- U8 pad 2: /3V3A -> /ATTEN_CLK
- U8 pad 25: GND -> (no net)
- U8 pad 3: /Source Leveling/nP_S -> /ATTEN_MOSI
- U8 pad 4: GND -> /ATTEN_LE
- U8 pad 5: /Source Leveling/RF_IN -> GND
- U8 pad 6: GND -> /Source Leveling/RF_IN
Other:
- copper layers 2 -> 4
- net class RF added: clearance 1, trace_width 0.293, via_dia 0.6, via_drill 0.3
- net class USB added: clearance 0.2, trace_width 0.26, via_dia 0.6, via_drill 0.3
- rule solder_mask_min_width: 0.25 -> 0.01
- rule trace_min: 0.2 -> 0.1
- rule via_min_drill: 0.3 -> 0.2
- rule via_min_size: 0.4 -> 0.45

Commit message: first day of layout / routing done
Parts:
- removed the FL1 at (121.5, 68.8)
- removed the FL2 at (112.1, 68.8)
- removed REF**: SLP3-150-150-F, VNA_Footprints:SLP3-150-150-F
- added C74: DNP, Capacitor_SMD:C_0402_1005Metric, F.Cu at (123.8, 103.2)
- added D18: LED, LED_SMD:LED_0603_1608Metric, F.Cu at (157.2, 117.9)
- added HY1: ADC-15-4+, VNA_Footprints:CD542, F.Cu at (168.8, 113.2)
- added HY2: ADC-15-4+, VNA_Footprints:CD542, F.Cu at (178.0, 109.3)
- added R62: DNP, Resistor_SMD:R_0402_1005Metric, F.Cu at (122.0, 103.2)
- added R63: 470R, Resistor_SMD:R_0603_1608Metric, F.Cu at (157.2, 116.3)
- added R64: DNP, Resistor_SMD:R_0603_1608Metric, F.Cu at (100.1, 71.0)
- added R65: 10K, Resistor_SMD:R_0603_1608Metric, F.Cu at (173.1, 72.3)
- added R66: 10K, Resistor_SMD:R_0603_1608Metric, F.Cu at (162.6, 72.3)
- F1: footprint VNA_Footprints:Fuse_1206_3216Metric -> VNA_Footprints:Fuse_0805_2012Metric
- FL1: renamed from FL3; value LFCN-105+ -> LFCN-225+
- FL2: renamed from FL4; value LFCN-225+ -> LFCN-400+
- FL3: renamed from FL5; value LFCN-400+ -> LFCN-1000+
- FL4: renamed from FL6; value LFCN-1000+ -> LFCN-1500+
- J4, J5: footprint VNA_Footprints:SMA_EDGE_MOUNT -> VNA_Footprints:SMA_EDGE_MOUNT_INSET
- Q1: footprint Package_TO_SOT_SMD:SOT-89-3 -> Package_TO_SOT_SMD:SOT-416
- TP1, TP10, TP17, TP18, TP19, TP2, TP20, TP21, TP22, TP23, TP24, TP25, TP26, TP27, TP28, TP29, TP3, TP30, TP31, TP32, TP33, TP34, TP35, TP36, TP37, TP38, TP39, TP4, TP40, TP41, TP42, TP44, TP5, TP6, TP7, TP8, TP9: moved to B.Cu
- moved D1 145.4 mm to (171.6, 98.7), turned to 180 degrees
- moved H2 143.2 mm to (186.2, 124.3)
- moved J4 139.5 mm to (186.2, 78.3)
- moved J5 138.0 mm to (186.2, 111.3)
- moved SW2 136.6 mm to (176.4, 67.8)
- moved H3 131.5 mm to (186.2, 65.3)
- moved SW1 126.5 mm to (165.9, 67.8)
- moved C67 120.9 mm to (148.8, 89.7)
- moved Q1 118.1 mm to (174.4, 101.0), turned to 90 degrees
- moved U16 117.8 mm to (139.4, 82.0), turned to 90 degrees
- moved Y1 116.9 mm to (137.9, 92.9), turned to 180 degrees
- moved R1 116.8 mm to (168.6, 98.7)
- moved U17 116.6 mm to (150.2, 96.2)
- moved C73 114.6 mm to (155.7, 94.3), turned to 180 degrees
- moved C69 111.6 mm to (149.4, 85.5), turned to 270 degrees
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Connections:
- C65 pad 1: VDD -> VDDA
- C66 pad 1: VDD -> VDDA
- C67 pad 1: VDD -> VDDA
- C68 pad 1: VDD -> VDDA
- C69 pad 1: VDDA -> VDD
- C70 pad 1: VDDA -> VDD
- C71 pad 1: VDDA -> VDD
- C72 pad 1: VDDA -> VDD
- R11 pad 1: Net-(C24-Pad2) -> Net-(C26-Pad1)
- R11 pad 2: Net-(C26-Pad1) -> Net-(C24-Pad2)
- U1 pad 1: /USB_D+ -> /USB_D-
- U1 pad 3: /Dp -> /Dn
- U1 pad 4: /Dn -> /Dp
- U1 pad 6: /USB_D- -> /USB_D+
- U14 pad 13: Net-(R38-Pad1) -> Net-(R37-Pad1)
- U14 pad 3: Net-(R37-Pad1) -> Net-(R38-Pad1)
- U8 pad 25: (no net) -> GND
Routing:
- net GND: track 0.00 -> 131.2 mm, vias 0 -> 134
- net /3V3A: track 0.00 -> 34.2 mm, vias 0 -> 14
- net Net-(C16-Pad1): track 0.00 -> 25.4 mm
- net VDD: track 0.00 -> 21.9 mm
- net /Filter_CTRL2: track 0.00 -> 19.7 mm, vias 0 -> 3
- net Net-(C24-Pad2): track 0.00 -> 18.1 mm, vias 0 -> 2
- net Net-(D10-Pad1): track 0.00 -> 14.4 mm
- net Net-(C20-Pad1): track 0.00 -> 12.2 mm
- net /Filter Bank/SW_2_CTRL_1: track 0.00 -> 10.8 mm, vias 0 -> 2
- net Net-(D9-Pad1): track 0.00 -> 10.5 mm
- net Net-(R66-Pad1): track 0.00 -> 10.5 mm
- net Net-(R65-Pad1): track 0.00 -> 10.4 mm
- net /5V0: track 0.00 -> 10.4 mm
- net Net-(D8-Pad1): track 0.00 -> 9.41 mm
- net /Filter_CTRL1: track 0.00 -> 8.94 mm, vias 0 -> 1
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- added copper zone on 3V3A, net /3V3A
- added copper zone on GND, net GND
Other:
- board outline added: 100 x 67 mm
- net class Default: clearance 0.2 -> 0.15; via_dia 0.8 -> 0.5; via_drill 0.4 -> 0.25
- net class RF: clearance 1 -> 0.2
- rule trace_clearance: 0.2 -> 0.15
- rule via_min_drill: 0.2 -> 0.25
- rule via_min_size: 0.45 -> 0.5

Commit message: more routing progress
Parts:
- removed TP29, TP30, TP39, TP40, TP42: TP, TestPoint:TestPoint_Pad_D1.0mm
- moved D3 58.9 mm to (131.4, 49.2)
- moved D4 58.9 mm to (131.4, 54.0)
- moved D1 58.9 mm to (131.4, 55.6)
- moved D5 58.9 mm to (131.4, 50.8)
- moved D6 58.9 mm to (131.4, 52.4)
- moved Q1 58.9 mm to (134.2, 57.9)
- moved R1 58.9 mm to (128.4, 55.6)
- moved R13 58.9 mm to (134.5, 59.9)
- moved R17 58.9 mm to (128.4, 50.8)
- moved R18 58.9 mm to (128.4, 52.4)
- moved D2 58.9 mm to (131.4, 57.2)
- moved R14 58.9 mm to (128.4, 57.2)
- moved R15 58.9 mm to (128.4, 49.2)
- moved R16 58.9 mm to (128.4, 54.0)
- moved TP23 21.9 mm to (101.5, 51.6)
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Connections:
- net /Dn renamed /D_N
- net /Dp renamed /D_P
- J6 pad 2: /UART_TX -> /UART_RX
- J6 pad 3: /UART_RX -> /UART_TX
- U16 pad 2: (no net) -> /ATTEN_MOSI
- U16 pad 26: /AD8302_VPHASE -> (no net)
- U16 pad 27: (no net) -> /RF_PWR_LEVEL
- U16 pad 28: /RF_PWR_LEVEL -> /AD8302_VMAG
- U16 pad 3: (no net) -> /ATTEN_CLK
- U16 pad 30: /AD8302_VMAG -> /AD8302_VPHASE
- U16 pad 51: /ATTEN_MOSI -> (no net)
- U16 pad 52: /ATTEN_CLK -> (no net)
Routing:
- net VDDA: track 0.00 -> 64.5 mm, vias 0 -> 3
- net /RF_PWR_LEVEL: track 0.00 -> 62.6 mm, vias 0 -> 2
- net /PA_PWRDN: track 0.00 -> 58.5 mm, vias 0 -> 2
- net /USB_D+: track 0.00 -> 49.4 mm
- net /USB_D-: track 0.00 -> 48.6 mm
- net /MAX2871_MISO: track 1.54 -> 47.9 mm, vias 1 -> 4
- net /MAX2871_MOSI: track 1.37 -> 47.1 mm, vias 1 -> 2
- net /MAX2871_CLK: track 0.55 -> 46.0 mm, vias 1 -> 2
- net /MAX2871_CHIP_EN: track 0.81 -> 45.8 mm, vias 1 -> 2
- net /MAX2871_LE: track 0.98 -> 45.4 mm, vias 1 -> 2
- net /ATTEN_LE: track 1.12 -> 44.1 mm, vias 1 -> 0
- net /MAX2871_RFOUT_EN: track 0.80 -> 43.0 mm, vias 1 -> 2
- net /MAX2871_LD: track 0.85 -> 40.3 mm, vias 1 -> 2
- net /ATTEN_MOSI: track 1.00 -> 35.1 mm, vias 1 -> 0
- net /ATTEN_CLK: track 0.98 -> 34.3 mm, vias 1 -> 0
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
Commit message: no unrouted nets!
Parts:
- Q1: footprint Package_TO_SOT_SMD:SOT-416 -> VNA_Footprints:SOT-416
- TP1, TP10, TP17, TP18, TP19, TP2, TP20, TP21, TP22, TP23, TP24, TP25, TP26, TP27, TP28, TP3, TP31, TP32, TP33, TP34, TP35, TP36, TP37, TP38, TP4, TP41, TP44, TP5, TP6, TP7, TP8, TP9: moved to F.Cu
- moved TP13 95.7 mm to (178.5, 115.8)
- moved TP6 87.6 mm to (160.7, 120.7)
- moved TP2 79.6 mm to (160.9, 103.6)
- moved TP34 76.2 mm to (157.5, 100.6)
- moved TP12 71.8 mm to (154.2, 103.6), turned to 90 degrees
- moved TP15 71.6 mm to (134.7, 118.6)
- moved TP44 69.4 mm to (146.9, 103.2)
- moved TP14 68.0 mm to (165.9, 88.9), turned to 90 degrees
- moved TP8 67.9 mm to (116.7, 117.1)
- moved TP20 67.8 mm to (155.9, 98.8)
- moved TP38 66.3 mm to (148.4, 104.8)
- moved D1 66.0 mm to (135.8, 121.5)
- moved R1 66.0 mm to (132.8, 121.5)
- moved TP27 65.8 mm to (145.4, 101.8)
- moved TP28 65.7 mm to (138.9, 102.1)
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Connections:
- SW1 pad 2: Net-(R66-Pad1) -> Net-(R65-Pad1)
- SW2 pad 2: Net-(R65-Pad1) -> Net-(R66-Pad1)
- U16 pad 35: /INPUT_SW_1 -> /INPUT_SW_2
- U16 pad 48: /ATTEN_MISO -> (no net)
- U16 pad 52: (no net) -> /ATTEN_MISO
- U2 pad 3: Net-(J2-Pad3) -> Net-(J2-Pad2)
- U2 pad 4: Net-(J2-Pad2) -> Net-(J2-Pad3)
- U5 pad 3: GND -> (no net)
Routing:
- net VDD: track 33.4 -> 250.0 mm, vias 0 -> 13
- net /5V0: track 10.4 -> 133.3 mm, vias 0 -> 8
- net GND: track 147.6 -> 225.2 mm, vias 157 -> 209
- net /Microcontroller/STATUS_LED_G: track 0.00 -> 73.9 mm, vias 0 -> 2
- net /SWD_nRST: track 0.00 -> 72.7 mm, vias 0 -> 4
- net /Microcontroller/STATUS_LED_B: track 0.00 -> 60.4 mm, vias 0 -> 4
- net /Microcontroller/STATUS_LED_R: track 0.00 -> 57.8 mm, vias 0 -> 4
- net /INPUT_SW_1: track 0.00 -> 57.0 mm, vias 0 -> 2
- net /INPUT_SW_2: track 0.00 -> 56.5 mm, vias 0 -> 2
- net /ATTEN_MISO: track 1.34 -> 51.9 mm, vias 1 -> 4
- net /SCL: track 0.00 -> 50.4 mm, vias 0 -> 3
- net /SDA: track 0.00 -> 42.3 mm, vias 0 -> 2
- net Net-(R66-Pad1): track 10.5 -> 52.7 mm
- net /1V8: track 7.66 -> 45.0 mm
- net /Filter_CTRL1: track 23.8 -> 55.6 mm
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- added copper zone on F.Cu, net /3V3A
- added copper zone on 3V3A, net /5V0
- added copper zone on F.Cu, net /5V0
- added copper zone on F.Cu, net GND
- added copper zone on 3V3A, net VDD
- added copper zone on F.Cu, net VDD
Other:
- rule trace_min: 0.1 -> 0.15
- board text added: "Lock Detect"
- board text added: "PA ON"
